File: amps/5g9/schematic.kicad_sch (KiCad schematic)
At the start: 68 parts, among them T1 8160, T2 108

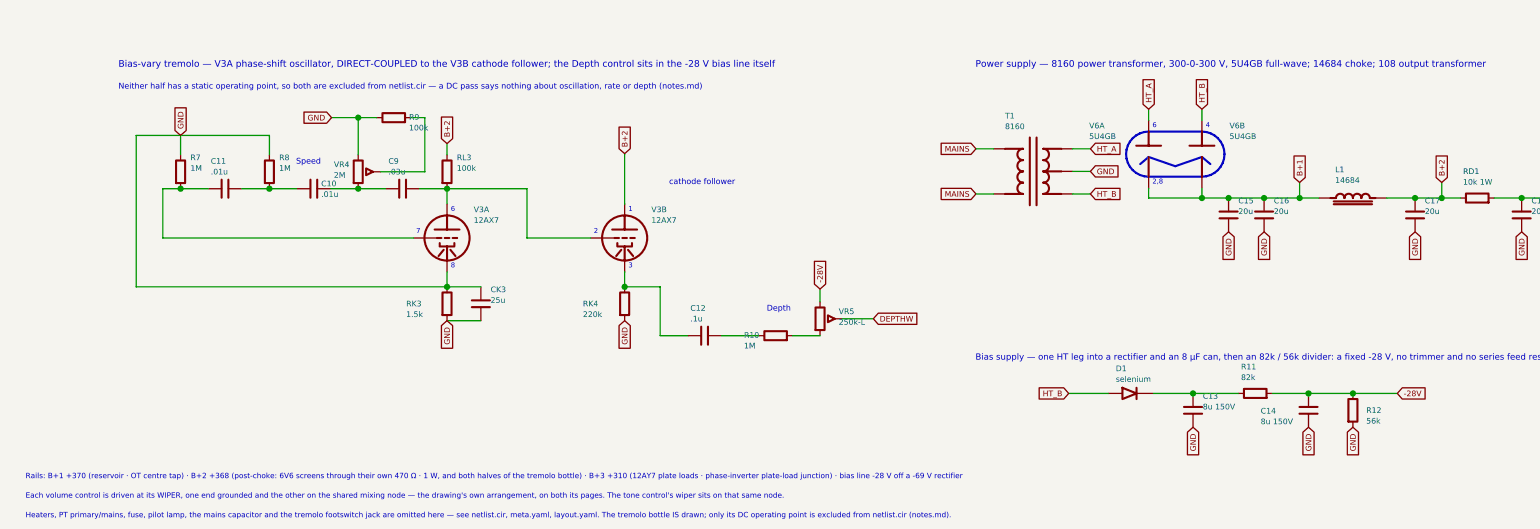
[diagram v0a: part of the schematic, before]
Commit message: Fix: schematic sheet notes no longer name repository files
Thirty-seven committed sheets rendered footnotes and section notes such as
"Heaters and PT primary omitted — see netlist.cir and meta.yaml" or
"excluded from netlist.cir (notes.md)" to visitors through KiCanvas. The
prose sweeps never counted sheets. Rewritten in the site's own words — the
netlist, the sources list, the circuit story, the parts list, the board
drawing — in 59 strings across 33 draw scripts, keeping every technical
claim as it was; the three tone sheets (6G4, 6G5, 6G6-B) are under repair
elsewhere and keep theirs for now. The sweep touched only strings passed to
the sheet's note, text, caption and footnote calls, never a path or a value.

Gates: check_schematics 40/0, connectivity 0 isolated pins;
verify_schematic_nets 40 clean; only the regenerated sheets and their served
copies changed.

Co-Authored-By: Claude Fable 5.1 <noreply@anthropic.com>
Claude-Session: https://claude.ai/code/session_01KBMfdh37HmCL2iWcBiL5J1
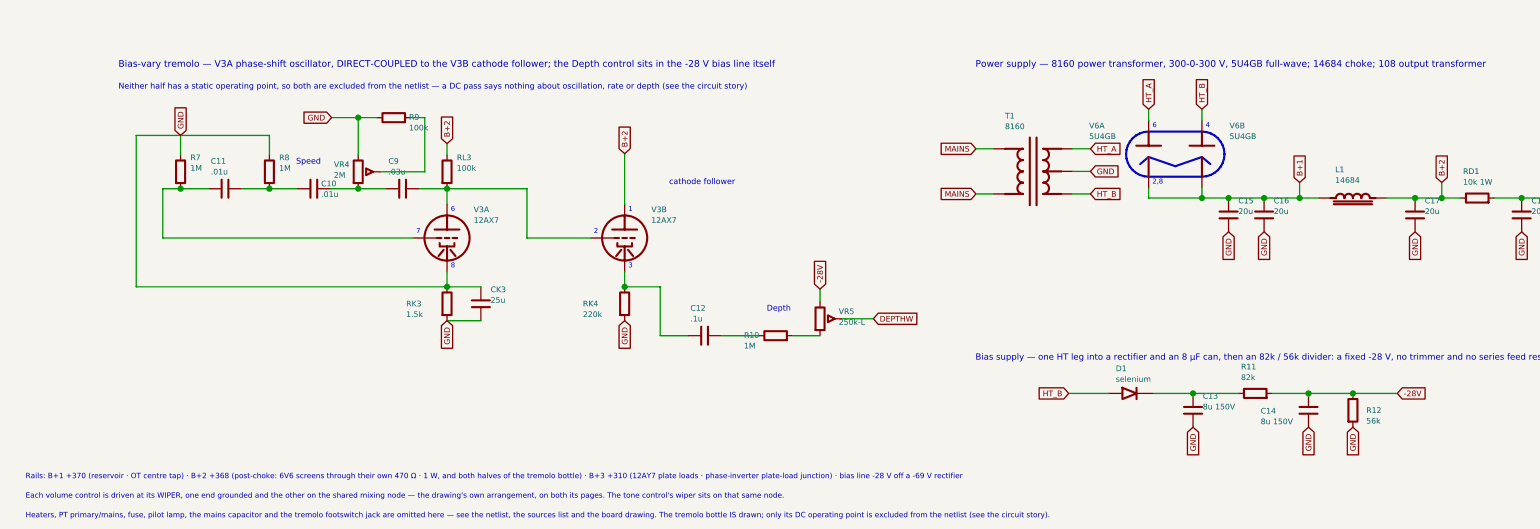
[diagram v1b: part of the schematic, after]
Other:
- note added: "Heaters, PT primary/mains, fuse, pilot lamp, the mains capacitor and the tremolo footswitch jack are omitted here — see the netlist, the sources list and the board drawing. The tremolo bottle IS drawn; only its DC operating point is excluded from the netlist (see the circuit story)."
- note added: "Neither half has a static operating point, so both are excluded from the netlist — a DC pass says nothing about oscillation, rate or depth (see the circuit story)"
- note removed: "Heaters, PT primary/mains, fuse, pilot lamp, the mains capacitor and the tremolo footswitch jack are omitted here — see netlist.cir, meta.yaml, layout.yaml. The tremolo bottle IS drawn; only its DC operating point is excluded from netlist.cir (notes.md)."
- note removed: "Neither half has a static operating point, so both are excluded from netlist.cir — a DC pass says nothing about oscillation, rate or depth (notes.md)"
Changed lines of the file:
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@@
   (text "Bias-vary tremolo — V3A phase-shift oscillator, DIRECT-COUPLED to the V3B cathode follower; the Depth control sits in the -28 V bias line itself" (at 33.6088 159.75 0)
     (effects (font (size 1.5 1.5)) (justify left)))
-  (text "Neither half has a static operating point, so both are excluded from netlist.cir — a DC pass says nothing about oscillation, rate or depth (notes.md)" (at 33.6088 164.75 0)
+  (text "Neither half has a static operating point, so both are excluded from the netlist — a DC pass says nothing about oscillation, rate or depth (see the circuit story)" (at 33.6088 164.75 0)
     (effects (font (size 1.3 1.3)) (justify left)))
   (symbol (lib_id "cx:TRIODE") (at 107.609 198.75 0) (unit 1)
@@
   (text "Each volume control is driven at its WIPER, one end grounded and the other on the shared mixing node — the drawing's own arrangement, on both its pages. The tone control's wiper sits on that same node." (at 12.7 256.928 0)
     (effects (font (size 1.2 1.2)) (justify left)))
-  (text "Heaters, PT primary/mains, fuse, pilot lamp, the mains capacitor and the tremolo footswitch jack are omitted here — see netlist.cir, meta.yaml, layout.yaml. The tremolo bottle IS drawn; only its DC operating point is excluded from netlist.cir (notes.md)." (at 12.7 261.328 0)
+  (text "Heaters, PT primary/mains, fuse, pilot lamp, the mains capacitor and the tremolo footswitch jack are omitted here — see the netlist, the sources list and the board drawing. The tremolo bottle IS drawn; only its DC operating point is excluded from the netlist (see the circuit story)." (at 12.7 261.328 0)
     (effects (font (size 1.2 1.2)) (justify left)))
   (sheet_instances (path "/" (page "1")))

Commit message: Fix: state the datasheet unit on 17 dual-triode sections whose sheets printed the other half's pin numbers
The sheet-vs-board gate reported these sockets as SECTION-SWAP; the
2026-09-10 source-read triage found the BOARD right on every one of them
(and both surfaces wrong on the 5G9 tremolo bottle). Each sheet had
lettered the section on the default map (A -> unit 1 -> pins 6/7/8) where
the factory drawing puts that stage on 1/2/3. The draw scripts now state
`unit=` on both halves, with the source cited beside the call, so the
printed socket numbers are the factory's:

- 5f4 V3: driver V3A -> 1/2/3, cathodyne V3B -> 6/7/8
  (crop 5f4-V3-layout-trace.png: +213 V driver plate -> pin 1, +270 V -> 6)
- 5f8a V3: 82k half V3A -> 1/2/3, 100k half V3B -> 6/7/8
  (crop 5f8a-V3-layout-trace.png: +225 -> 6, +19 -> 2, +28.5 -> 8)
- 6161 V1: channel 1 V1A -> 1/2/3 (crop 6161-V1-ch1.png prints 1/2/3);
  6161 V2: 1 MEG-grid half V2A -> 1/2/3, paraphase V2B -> 6/7/8
  (crop 6161-V2.png / 6161-V2-right.png)
- 6g3 V3: 82k half V3A -> 1/2/3 (crop 6g3-V3-layout-wires.png: +230 -> 1,
  +225 -> 6, +20 -> 7)
- aa1164 V3: recovery V3A -> 1/2/3, mixer V3B -> 6/7/8
  (crops aa1164-V3A-recovery-schem.png, aa1164-V3B-mixer-schem.png)
- aa864-bassman V1/V2: input stages 2/1/3, second stages 7/6/8; V4: the
  .1/500 pF-fed 82k half 2/1/3 (crops aa864-V1A-input.png,
  aa864-V1B-second.png, aa864-V2A-input.png, aa864-V2B-second.png,
  aa864-V4-PI.png)
- ab165 V1/V2/V4: same pattern (crops ab165-V1A-input.png,
  ab165-V1B-second.png, ab165-V2A-input.png, ab165-V2B-second.png,
  ab165-V4-PI.png)
- ab763-super V1/V2: slope-plate +270 V -> pin 1 (input stage), .047
  plate -> 6 (crops ab763-super-V1-layout-sh.png, ab763-super-V2-layout-sh.png)
- dr103 V2/V3: gain stages 6/7/8, cathode followers 1/2/3 (crops
  dr103-V2-huss.png, dr103-V3-huss.png — the Huss redraw, not a factory
  print; noted in the script)
- 5g9 V3: oscillator V3A -> 1/2/3, follower V3B -> 6/7/8 (crops
  5g9-V3-strap71-zoom.png, 5g9-V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
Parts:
- V3A: Basing_unit (none) -> 2
- V3B: Basing_unit (none) -> 1
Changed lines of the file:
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@@
     (in_bom yes) (on_board yes)
     (property "Reference" "V3A" (at 113.609 192.35 0) (effects (font (size 1.27 1.27)) (justify left)))
-    (property "Value" "12AX7" (at 113.609 194.75 0) (effects (font (size 1.27 1.27)) (justify left))))
+    (property "Value" "12AX7" (at 113.609 194.75 0) (effects (font (size 1.27 1.27)) (justify left)))
+    (property "Basing_unit" "2" (at 113.609 197.15 0) (effects (font (size 1.27 1.27)) hide)))
   (wire (pts (xy 107.609 191.13) (xy 107.609 187.65))
     (stroke (width 0) (type default)))
@@
     (in_bom yes) (on_board yes)
     (property "Reference" "V3B" (at 153.609 192.35 0) (effects (font (size 1.27 1.27)) (justify left)))
-    (property "Value" "12AX7" (at 153.609 194.75 0) (effects (font (size 1.27 1.27)) (justify left))))
+    (property "Value" "12AX7" (at 153.609 194.75 0) (effects (font (size 1.27 1.27)) (justify left)))
+    (property "Basing_unit" "1" (at 153.609 197.15 0) (effects (font (size 1.27 1.27)) hide)))
   (wire (pts (xy 125.609 198.75) (xy 139.989 198.75))
     (stroke (width 0) (type default)))
@@
   (text "8" (at 218.459 99.465 0)
     (effects (font (size 1.1 1.1)) (justify left)))
-  (text "6" (at 108.459 192.4 0)
-    (effects (font (size 1.1 1.1)) (justify left)))
-  (text "7" (at 100.662 197.35 0)
-    (effects (font (size 1.1 1.1)) (justify left)))
-  (text "8" (at 108.459 205.1 0)
-    (effects (font (size 1.1 1.1)) (justify left)))
-  (text "1" (at 148.459 192.4 0)
-    (effects (font (size 1.1 1.1)) (justify left)))
-  (text "2" (at 140.662 197.35 0)
-    (effects (font (size 1.1 1.1)) (justify left)))
-  (text "3" (at 148.459 205.1 0)
+  (text "1" (at 108.459 192.4 0)
+    (effects (font (size 1.1 1.1)) (justify left)))
+  (text "2" (at 100.662 197.35 0)
+    (effects (font (size 1.1 1.1)) (justify left)))
+  (text "3" (at 108.459 205.1 0)
+    (effects (font (size 1.1 1.1)) (justify left)))
+  (text "6" (at 148.459 192.4 0)
+    (effects (font (size 1.1 1.1)) (justify left)))
+  (text "7" (at 140.662 197.35 0)
+    (effects (font (size 1.1 1.1)) (justify left)))
+  (text "8" (at 148.459 205.1 0)
     (effects (font (size 1.1 1.1)) (justify left)))
   (text "6" (at 266.459 173.52 0)

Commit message: Fix: feed the tweed bias rectifiers from the transformer's bias tap, not a rectifier plate (5E4-A, 5E5-A, 5F4, 5G9)
The 8087-family power transformer brings out a BIAS TAP on the HT winding,
between one end and the centre tap — the layouts letter that lead RED-BLUE
— and every fixed-bias tweed factory sheet draws the bias rectifier from
that fourth winding terminal. These four sheets drew it from a rectifier
plate (the HT_B label). The boards carry the same mistake, which is why the
sheet-vs-board gate could not see it; the source read did.

cx:PT gains an OPTIONAL pin 6, HT_TAP, between HT_A and the centre tap.
`s.pt(..., tap=True)` asks for it, and only that sheet's embedded library
carries the pin (lib_text(pt_tap=...)), so every sheet that does not wire
it is byte-identical — proved by the regenerate-all diff below. The
contract tables (SYM_EXTENTS/SYM_PINS) are built with the pin so the lint
and the wire-cutting know it; the tap lies inside the symbol's box, so no
extent moves.

- 5g9: T1 8160 drawn with the tap (moved 8 mm left for the label), the
  selenium rectifier's AC side on HT_TAP (crop 5g9-D1-schem.png: the
  rectifier + runs straight to a winding terminal between the 300 V AC end
  and the centre tap; layout: a separate lead to SEL. RECT. +).
- 5e4a, 5f4: these sheets drew no PT at all, so a T1 is added (MAINS labels
  on the primary, HT_A / HT_TAP / centre tap / HT_B on the secondary, the
  same idiom the 5G9 uses), the 18k / 6800 bias feed taken from HT_TAP,
  and T1 added to bom.yaml (crops 5e4a-D1-schem.png, 5f4-D1-schem.png:
  the series resistor from a winding terminal between the top end and the
  centre tap; 5e4a-D1-layout.png: RED-BLUE lead to the selenium +).
- 5e5a: T1 added the same way; the bias row now carries the factory's 10 K
  in series from the tap into the cell and the 56 K bleeder across the
  100 µF can (crop 5e5a-D1-schem.png), both added to bom.yaml (RB1, RB2)
  — the board places neither, so they report SHEET-ONLY until it doe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
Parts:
- removed C13: 8u 150V, symbol cx:C
- added R11: 82k, symbol cx:R
- C13: renamed from R11; value 82k -> 8u 150V; symbol cx:R -> cx:C
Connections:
- net -28V: now also R11.2; no longer C13.2
- net GND: now also C13.2
- net HT_B: no longer D1.1 (A)
- net at C13.1, D1.2 (K): now also R11.1
- new net HT_TAP: D1.1 (A), T1.6 (HT_TAP)
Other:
- note added: "Bias supply — the winding's bias tap into a rectifier and an 8 µF can, then an 82k / 56k divider: a fixed -28 V; no trimmer, no series feed"
- note removed: "Bias supply — one HT leg into a rectifier and an 8 µF can, then an 82k / 56k divider: a fixed -28 V, no trimmer and no series feed resistor"
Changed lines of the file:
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@@
   (text "Power supply — 8160 power transformer, 300-0-300 V, 5U4GB full-wave; 14684 choke; 108 output transformer" (at 226.609 159.75 0)
     (effects (font (size 1.5 1.5)) (justify left)))
-  (symbol (lib_id "cx:PT") (at 239.609 183.75 0) (unit 1)
+  (symbol (lib_id "cx:PT") (at 231.609 183.75 0) (unit 1)
     (in_bom yes) (on_board yes)
-    (property "Reference" "T1" (at 233.259 171.25 0) (effects (font (size 1.27 1.27)) (justify left)))
-    (property "Value" "8160" (at 233.259 173.65 0) (effects (font (size 1.27 1.27)) (justify left))))
-  (wire (pts (xy 230.719 178.67) (xy 226.719 178.67))
+    (property "Reference" "T1" (at 225.259 171.25 0) (effects (font (size 1.27 1.27)) (justify left)))
+    (property "Value" "8160" (at 225.259 173.65 0) (effects (font (size 1.27 1.27)) (justify left))))
+  (wire (pts (xy 222.719 178.67) (xy 218.719 178.67))
     (stroke (width 0) (type default)))
-  (global_label "MAINS" (shape input) (at 226.719 178.67 180)
+  (global_label "MAINS" (shape input) (at 218.719 178.67 180)
     (effects (font (size 1.27 1.27)) (justify right)))
-  (wire (pts (xy 230.719 188.83) (xy 226.719 188.83))
+  (wire (pts (xy 222.719 188.83) (xy 218.719 188.83))
     (stroke (width 0) (type default)))
-  (global_label "MAINS" (shape input) (at 226.719 188.83 180)
+  (global_label "MAINS" (shape input) (at 218.719 188.83 180)
     (effects (font (size 1.27 1.27)) (justify right)))
-  (wire (pts (xy 248.499 178.67) (xy 252.499 178.67))
+  (wire (pts (xy 240.499 178.67) (xy 250.499 178.67))
     (stroke (width 0) (type default)))
-  (global_label "HT_A" (shape input) (at 252.499 178.67 0)
+  (global_label "HT_A" (shape input) (at 250.499 178.67 0)
     (effects (font (size 1.27 1.27)) (justify left)))
-  (wire (pts (xy 248.499 188.83) (xy 252.499 188.83))
+  (wire (pts (xy 240.499 181.21) (xy 242.499 181.21))
     (stroke (width 0) (type default)))
-  (global_label "HT_B" (shape input) (at 252.499 188.83 0)
+  (global_label "HT_TAP" (shape input) (at 242.499 181.21 0)
     (effects (font (size 1.27 1.27)) (justify left)))
-  (wire (pts (xy 248.499 183.75) (xy 252.499 183.75))
+  (wire (pts (xy 240.499 188.83) (xy 244.499 188.83))
     (stroke (width 0) (type default)))
-  (global_label "GND" (shape input) (at 252.499 183.75 0)
+  (global_label "HT_B" (shape input) (at 244.499 188.83 0)
+    (effects (font (size 1.27 1.27)) (justify left)))
+  (wire (pts (xy 240.499 183.75) (xy 250.499 183.75))
+    (stroke (width 0) (type default)))
+  (global_label "GND" (shape input) (at 250.499 183.75 0)
     (effects (font (size 1.27 1.27)) (justify left)))
   (global_label "HT_A" (shape input) (at 265.609 169.75 90)
@@
   (global_label "B+3" (shape input) (at 355.609 186.25 90)
     (effects (font (size 1.27 1.27)) (justify left)))
-  (text "Bias supply — one HT leg into a rectifier and an 8 µF can, then an 82k / 56k divider: a fixed -28 V, no trimmer and no series feed resistor" (at 226.609 225.75 0)
+  (text "Bias supply — the winding's bias tap into a rectifier and an 8 µF can, then an 82k / 56k divider: a fixed -28 V; no trimmer, no series feed" (at 226.609 225.75 0)
     (effects (font (size 1.4 1.4)) (justify left)))
-  (global_label "HT_B" (shape input) (at 247.609 233.75 180)
+  (global_label "HT_TAP" (shape input) (at 247.609 233.75 180)
     (effects (font (size 1.27 1.27)) (justify right)))
   (wire (pts (xy 247.609 233.75) (xy 256.529 233.75))

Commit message: Fix: four single-sheet faults — 5G9 oscillator cathode grounded, B15N R36 bridging both rectifier plates, M1959/M1987 bias series resistor drawn as a shunt / after the diode
- 5g9: the factory sheet (crop 5g9-V3-schem.png) prints the oscillator
  cathode at +1.7 V on 1500 ‖ 25 µF, with the ladder's second 1M returned
  to that cathode node. The sheet had the same parts, but R7's ground flag
  stood ON the wire that returns R8 to the cathode, which grounded the
  whole node: RK3, CK3 and R8 all reported "the sheet shorts its two ends
  onto one net". The flag now points left from a shorter stub, clear of
  that wire. No part added — bom.yaml already carried RK3/CK3/R8.
- b15n: the Ampeg 591722 sheet (crop b15n-V6-rect.png, re-read at native
  resolution: R36's lower lead HOPS the B+ and screen lines and lands on
  the R35/D1 node with a dot) hangs R36 100K/2W on the pin-4 RED HT end.
  The sheet's feed wire ran from V6A's plate stub straight across the top
  of V6B's, joining both HT ends into one net (the SPLIT finding). R36 now
  takes its own HTA label. Caption reworded to name pin 4.
- m1959: the Unicord 70-6-11 sheet (crops m1959-bias-series.png,
  m1959-psu.png) runs the HT winding's end through the 27K (22K annotated)
  IN SERIES into the 1008 diode; the sheet drew it as a shunt at the
  diode. RBA is now in series before D1; bom role and circuit story
  reworded. The brief's "C24 on the bias node" does not exist on this
  amp: its bias filters are C17/C18 on sheet and BOM alike, C24 is the PI
  filter on both. The C24 on a bias-diode node was the M1987's rectifier
  snubber (below).
- m1987: the Unicord 70-19-11 sheet (crops m1987-bias.png, m1987-psu.png)
  runs the winding end through 220K into the diode, then 8 µF / 15K; the
  sheet had the diode first and the 220K after it, so RBA and RBB shared
  a node. RBA now sits before D1; RBA and RBB are separated by the diode.
  C24 (the D3 snubber, per bom.yaml) stays on HT_B and no longer shares a
  node with the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
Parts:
- removed CK3: 25u, symbol cx:C
- added RK3: 1.5k, symbol cx:R
- CK3: renamed from RK3; value 1.5k -> 25u; symbol cx:R -> cx:C
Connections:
- net GND: now also RK3.2; no longer CK3.1, R8.1, V3A.3 (K)
- new net: CK3.1, R8.1, RK3.1, V3A.3 (K)
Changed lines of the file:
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@@
   (wire (pts (xy 67.6088 180.03) (xy 67.6088 175.65))
     (stroke (width 0) (type default)))
-  (wire (pts (xy 67.6088 175.65) (xy 47.6088 175.65))
-    (stroke (width 0) (type default)))
-  (wire (pts (xy 47.6088 175.65) (xy 37.6088 175.65))
+  (wire (pts (xy 67.6088 175.65) (xy 37.6088 175.65))
     (stroke (width 0) (type default)))
   (wire (pts (xy 37.6088 175.65) (xy 37.6088 209.75))
@@
     (property "Reference" "R7" (at 49.8088 180.64 0) (effects (font (size 1.27 1.27)) (justify left)))
     (property "Value" "1M" (at 49.8088 183.04 0) (effects (font (size 1.27 1.27)) (justify left))))
-  (wire (pts (xy 47.6088 180.03) (xy 47.6088 175.65))
+  (wire (pts (xy 47.6088 180.03) (xy 47.6088 177.65))
     (stroke (width 0) (type default)))
-  (global_label "GND" (shape input) (at 47.6088 175.65 90)
-    (effects (font (size 1.27 1.27)) (justify left)))
+  (global_label "GND" (shape input) (at 47.6088 177.65 180)
+    (effects (font (size 1.27 1.27)) (justify right)))
   (wire (pts (xy 47.6088 187.65) (xy 43.6088 187.65))
     (stroke (width 0) (type default)))
